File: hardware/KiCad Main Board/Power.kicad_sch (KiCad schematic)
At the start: 57 parts, among them J9 Batt_Conn, Q2 AO3401A, Q3 AO3400A, Q4 AO3400A, Q5 AO3400A, Q6 AO3400A, U10 LM5157RTER, U13 NCP1117-1.8_SOT223, U2 S-8252ACP-M6T1U, U4 AP63203WU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

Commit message: added shunt resistors on 1V8 rail to comply with 1117 minimum load
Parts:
- added R10, R11: 100, Resistor_SMD:R_0603_1608Metric_Pad0.98x0.95mm_HandSolder, symbol Device:R_Small
- C98: footprint Capacitor_SMD:C_0603_1608Metric_Pad1.08x0.95mm_HandSolder -> Capacitor_SMD:C_0402_1005Metric_Pad0.74x0.62mm_HandSolder
- U13: value NCP1117-1.8_SOT223 -> AMS1117-1.8
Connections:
- net 1V8_AUDIO: now also R10.2
- net GND: now also R11.1
- new net: R10.1, R11.2
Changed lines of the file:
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@@
 	)
 	(junction
+		(at 259.08 55.88)
+		(diameter 0)
+		(color 0 0 0 0)
+	)
+	(junction
 		(at 149.86 69.85)
 		(diameter 0)
@@
 	)
 	(junction
+		(at 246.38 63.5)
+		(diameter 0)
+		(color 0 0 0 0)
+	)
+	(junction
 		(at 33.02 91.44)
 		(diameter 0)
@@
 	(wire
 		(pts
+			(xy 259.08 55.88) (xy 259.08 58.42)
+		)
+		(stroke
+			(width 0)
+			(type default)
+		)
+	)
+	(wire
+		(pts
 			(xy 133.35 97.79) (xy 133.35 99.06)
 		)
@@
 	(wire
 		(pts
+			(xy 246.38 63.5) (xy 247.65 63.5)
+		)
+		(stroke
+			(width 0)
+			(type default)
+		)
+	)
+	(wire
+		(pts
 			(xy 252.73 39.37) (xy 222.25 39.37)
 		)
@@
 	(wire
 		(pts
+			(xy 259.08 55.88) (xy 261.62 55.88)
+		)
+		(stroke
+			(width 0)
+			(type default)
+		)
+	)
+	(wire
+		(pts
 			(xy 43.18 118.11) (xy 48.26 118.11)
 		)
@@
 	(wire
 		(pts
+			(xy 259.08 63.5) (xy 259.08 64.77)
+		)
+		(stroke
+			(width 0)
+			(type default)
+		)
+	)
+	(wire
+		(pts
 			(xy 246.38 130.81) (xy 246.38 132.08)
 		)
@@
 	(wire
 		(pts
+			(xy 246.38 69.85) (xy 246.38 63.5)
+		)
+		(stroke
+			(width 0)
+			(type default)
+		)
+	)
+	(wire
+		(pts
 			(xy 222.25 137.16) (xy 219.71 137.16)
 		)
@@
 	(wire
 		(pts
+			(xy 259.08 69.85) (xy 246.38 69.85)
+		)
+		(stroke
+			(width 0)
+			(type default)
+		)
+	)
+	(wire
+		(pts
 			(xy 218.44 63.5) (xy 218.44 66.04)
 		)
@@
 	(wire
 		(pts
-			(xy 237.49 63.5) (xy 247.65 63.5)
+			(xy 237.49 63.5) (xy 246.38 63.5)
 		)
 		(stroke
@@
 	(wire
 		(pts
-			(xy 247.65 55.88) (xy 261.62 55.88)
+			(xy 247.65 55.88) (xy 259.08 55.88)
 		)
 		(stroke
@@
 			)
 		)
-		(property "Footprint" "Capacitor_SMD:C_0603_1608Metric_Pad1.08x0.95mm_HandSolder"
+		(property "Footprint" "Capacitor_SMD:C_0402_1005Metric_Pad0.74x0.62mm_HandSolder"
 			(at 237.49 30.48 0)
 			(effects
@@
 	)
 	(symbol
+		(lib_id "Device:R_Small")
+		(at 259.08 67.31 180)
+		(unit 1)
+		(exclude_from_sim no)
+		(in_bom yes)
+		(on_board yes)
+		(dnp no)
+		(fields_autoplaced yes)
+		(property "Reference" "R11"
+			(at 261.62 66.0399 0)
+			(effects
+				(font
+					(size 1.27 1.27)
+				)
+				(justify right)
+			)
+		)
+		(property "Value" "100"
+			(at 261.62 68.5799 0)
+			(effects
+				(font
+					(size 1.27 1.27)
+				)
+				(justify right)
+			)
+		)
+		(property "Footprint" "Resistor_SMD:R_0603_1608Metric_Pad0.98x0.95mm_HandSolder"
+			(at 259.08 67.31 0)
+			(effects
+				(font
+					(size 1.27 1.27)
+				)
+				(hide yes)
+			)
+		)
+		(property "Datasheet" "~"
+			(at 259.08 67.31 0)
+			(effects
+				(font
+					(size 1.27 1.27)
+				)
+				(hide yes)
+			)
+		)
+		(property "Description" "Resistor, small symbol"
+			(at 259.08 67.31 0)
+			(effects
+				(font
+					(size 1.27 1.27)
+				)
+				(hide yes)
+			)
+		)
+		(pin "1"
+		)
+		(pin "2"
+		)
+		(instances
+			(project "OSS Radio Hardware Design"
+				(path "/fd5c68a7-f5d0-4135-a258-bde3ebf63307/c701d20d-e266-4c46-aeb3-ff3d813a359d"
+					(reference "R11")
+					(unit 1)
+				)
+			)
+		)
+	)
+	(symbol
 		(lib_id "Diode:B340")
 		(at 31.75 21.59 180)
@@
 	)
 	(symbol
+		(lib_id "Device:R_Small")
+		(at 259.08 60.96 180)
+		(unit 1)
+		(exclude_from_sim no)
+		(in_bom yes)
+		(on_board yes)
+		(dnp no)
+		(fields_autoplaced yes)
+		(property "Reference" "R10"
+			(at 261.62 59.6899 0)
+			(effects
+				(font
+					(size 1.27 1.27)
+				)
+				(justify right)
+			)
+		)
+		(property "Value" "100"
+			(at 261.62 62.2299 0)
+			(effects
+				(font
+					(size 1.27 1.27)
+				)
+				(justify right)
+			)
+		)
+		(property "Footprint" "Resistor_SMD:R_0603_1608Metric_Pad0.98x0.95mm_HandSolder"
+			(at 259.08 60.96 0)
+			(effects
+				(font
+					(size 1.27 1.27)
+				)
+				(hide yes)
+			)
+		)
+		(property "Datasheet" "~"
+			(at 259.08 60.96 0)
+			(effects
+				(font
+					(size 1.27 1.27)
+				)
+				(hide yes)
+			)
+		)
+		(property "Description" "Resistor, small symbol"
+			(at 259.08 60.96 0)
+			(effects
+				(font
+					(size 1.27 1.27)
+				)
+				(hide yes)
+			)
+		)
+		(pin "1"
+		)
+		(pin "2"
+		)
+		(instances
+			(project "OSS Radio Hardware Design"
+				(path "/fd5c68a7-f5d0-4135-a258-bde3ebf63307/c701d20d-e266-4c46-aeb3-ff3d813a359d"
+					(reference "R10")
+					(unit 1)
+				)
+			)
+		)
+	)
+	(symbol
 		(lib_id "Diode:B340")
 		(at 143.51 45.72 180)
@@
 			)
 		)
-		(property "Value" "NCP1117-1.8_SOT223"
+		(property "Value" "AMS1117-1.8"
 			(at 218.44 52.07 0)
 			(effects
@@
 			)
 		)
-		(property "Datasheet" "http://www.onsemi.com/pub_link/Collateral/NCP1117-D.PDF"
+		(property "Datasheet" "AMS1117-1.8"
 			(at 220.98 62.23 0)
 			(effects

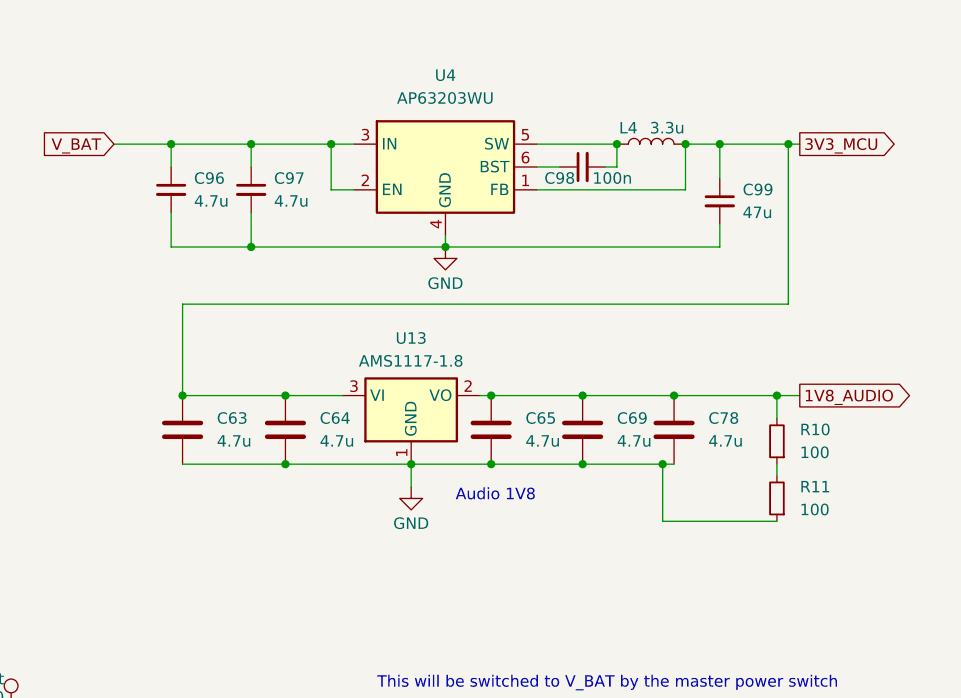
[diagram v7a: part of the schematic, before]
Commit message: made audio amp power swichable
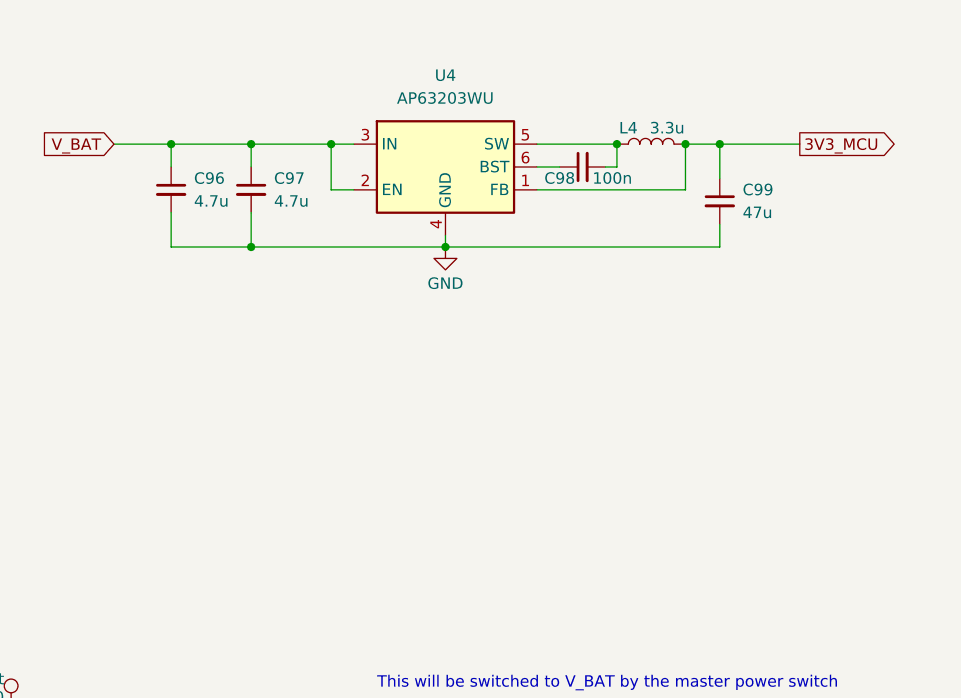
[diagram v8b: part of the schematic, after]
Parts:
- removed C63, C64, C65, C69, C78: 4.7u, Capacitor_SMD:C_0603_1608Metric_Pad1.08x0.95mm_HandSolder, symbol Device:C
- removed R10, R11: 100, Resistor_SMD:R_0603_1608Metric_Pad0.98x0.95mm_HandSolder, symbol Device:R_Small
- removed U13: AMS1117-1.8, Package_TO_SOT_SMD:SOT-223-3_TabPin2, symbol Regulator_Linear:NCP1117-1.8_SOT223
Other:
- note removed: "Audio 1V8"
